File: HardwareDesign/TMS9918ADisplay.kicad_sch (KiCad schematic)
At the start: 21 parts, among them J701 Conn_01x02, Q701 2N4401, U701 TMS9918A, U702 74HCT04, U703 74HCT00, U704 74HCT574, U705 74HCT574, U706 74HCT574, U707 HM62256BLP-7, Y701 10.738635 MHz

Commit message: fix connections to data bus
TI stupidly uses "CD0" to mean the *most* significant bit of
the data bus, which is completely backwards.
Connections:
- net D0: now also U701.17 (CD7); no longer U701.24 (CD0)
- net D1: now also U701.18 (CD6); no longer U701.23 (CD1)
- net D2: now also U701.19 (CD5); no longer U701.22 (CD2)
- net D3: now also U701.20 (CD4); no longer U701.21 (CD3)
- net D4: now also U701.21 (CD3); no longer U701.20 (CD4)
- net D5: now also U701.22 (CD2); no longer U701.19 (CD5)
- net D6: now also U701.23 (CD1); no longer U701.18 (CD6)
- net D7: now also U701.24 (CD0); no longer U701.17 (CD7)

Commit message: prepare to create PCB for TMS9918A module
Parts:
- removed J701: Conn_01x02, symbol Connector_Generic:Conn_01x02
- added J701: RCJ-044, CUI_RCJ-044:CUI_RCJ-044, symbol RCJ-044:RCJ-044
- C701, C702, C703, C704, C705, C706, C707, C710, C711: footprint (none) -> Capacitor_THT:C_Disc_D3.4mm_W2.1mm_P2.50mm
- Q701: footprint (none) -> Package_TO_SOT_THT:TO-92_HandSolder
- R701, R702: footprint (none) -> Resistor_THT:R_Axial_DIN0207_L6.3mm_D2.5mm_P7.62mm_Horizontal
- U701: footprint (none) -> Package_DIP:DIP-40_W25.4mm_Socket
- U702, U703: footprint (none) -> Package_DIP:DIP-14_W7.62mm_Socket
- U704, U705, U706: footprint (none) -> Package_DIP:DIP-20_W7.62mm_Socket
- U707: footprint DIP28 -> Package_DIP:DIP-28_W7.62mm_Socket
- Y701: footprint (none) -> Crystal:Crystal_HC18-U_Vertical
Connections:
- net GND: now also J701.1
- net at Q701.1 (E), R702.1: now also J701.2

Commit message: add support for VDP interrupt
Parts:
- added J702: Conn_01x02, symbol Connector_Generic:Conn_01x02
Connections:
- net at U701.16 (~{INT}): now also J702.2 (Pin_2)
- new net ~{VDPINT}: J702.1 (Pin_1)
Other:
- note added: "Use a shorting block to connect VDP's interrupt output to a system IRQ input"
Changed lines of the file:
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@@
+    (stroke (width 0) (type default) (color 0 0 0 0))
+  )
+  (wire (pts (xy 50.8 71.12) (xy 36.83 71.12))
     (stroke (width 0) (type default) (color 0 0 0 0))
   )
@@
     (stroke (width 0) (type default) (color 0 0 0 0))
   )
+  (wire (pts (xy 26.67 24.13) (xy 36.83 24.13))
+    (stroke (width 0) (type default) (color 0 0 0 0))
+  )
   (wire (pts (xy 50.8 158.75) (xy 57.15 158.75))
     (stroke (width 0) (type default) (color 0 0 0 0))
@@
   )
   (wire (pts (xy 26.67 45.72) (xy 50.8 45.72))
+    (stroke (width 0) (type default) (color 0 0 0 0))
+  )
+  (wire (pts (xy 36.83 71.12) (xy 36.83 26.67))
     (stroke (width 0) (type default) (color 0 0 0 0))
   )
@@
     (effects (font (size 1.27 1.27)) (justify left bottom))
   )
+  (text "Use a shorting block to\nconnect VDP's interrupt output\nto a system IRQ input"
+    (at 30.48 20.32 0)
+    (effects (font (size 1.27 1.27)) (justify left bottom))
+  )
   (label "VA6" (at 171.45 105.41 0)
     (effects (font (size 1.27 1.27)) (justify left bottom))
@@
   )
   (hierarchical_label "D0" (shape bidirectional) (at 26.67 55.88 180)
+    (effects (font (size 1.27 1.27)) (justify right))
+  )
+  (hierarchical_label "~{VDPINT}" (shape output) (at 26.67 24.13 180)
     (effects (font (size 1.27 1.27)) (justify right))
   )
@@
     (pin "7")
   )
+  (symbol (lib_id "Connector_Generic:Conn_01x02") (at 41.91 24.13 0) (unit 1)
+    (in_bom yes) (on_board yes) (fields_autoplaced)
+    (property "Reference" "J702" (id 0) (at 44.45 24.1299 0)
+      (effects (font (size 1.27 1.27)) (justify left))
+    )
+    (property "Value" "Conn_01x02" (id 1) (at 44.45 26.6699 0)
+      (effects (font (size 1.27 1.27)) (justify left))
+    )
+    (property "Footprint" "" (id 2) (at 41.91 24.13 0)
+      (effects (font (size 1.27 1.27)) hide)
+    )
+    (property "Datasheet" "~" (id 3) (at 41.91 24.13 0)
+      (effects (font (size 1.27 1.27)) hide)
+    )
+    (pin "1")
+    (pin "2")
+  )
   (symbol (lib_id "74xx:74HCT00") (at 64.77 156.21 0) (unit 3)

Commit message: footprint for VDP interrupt enable jumper
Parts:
- J702: footprint (none) -> Connector_PinHeader_2.54mm:PinHeader_1x02_P2.54mm_Vertical
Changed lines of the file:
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@@
       (effects (font (size 1.27 1.27)) (justify left))
     )
-    (property "Footprint" "" (id 2) (at 41.91 24.13 0)
+    (property "Footprint" "Connector_PinHeader_2.54mm:PinHeader_1x02_P2.54mm_Vertical" (id 2) (at 41.91 24.13 0)
       (effects (font (size 1.27 1.27)) hide)
     )

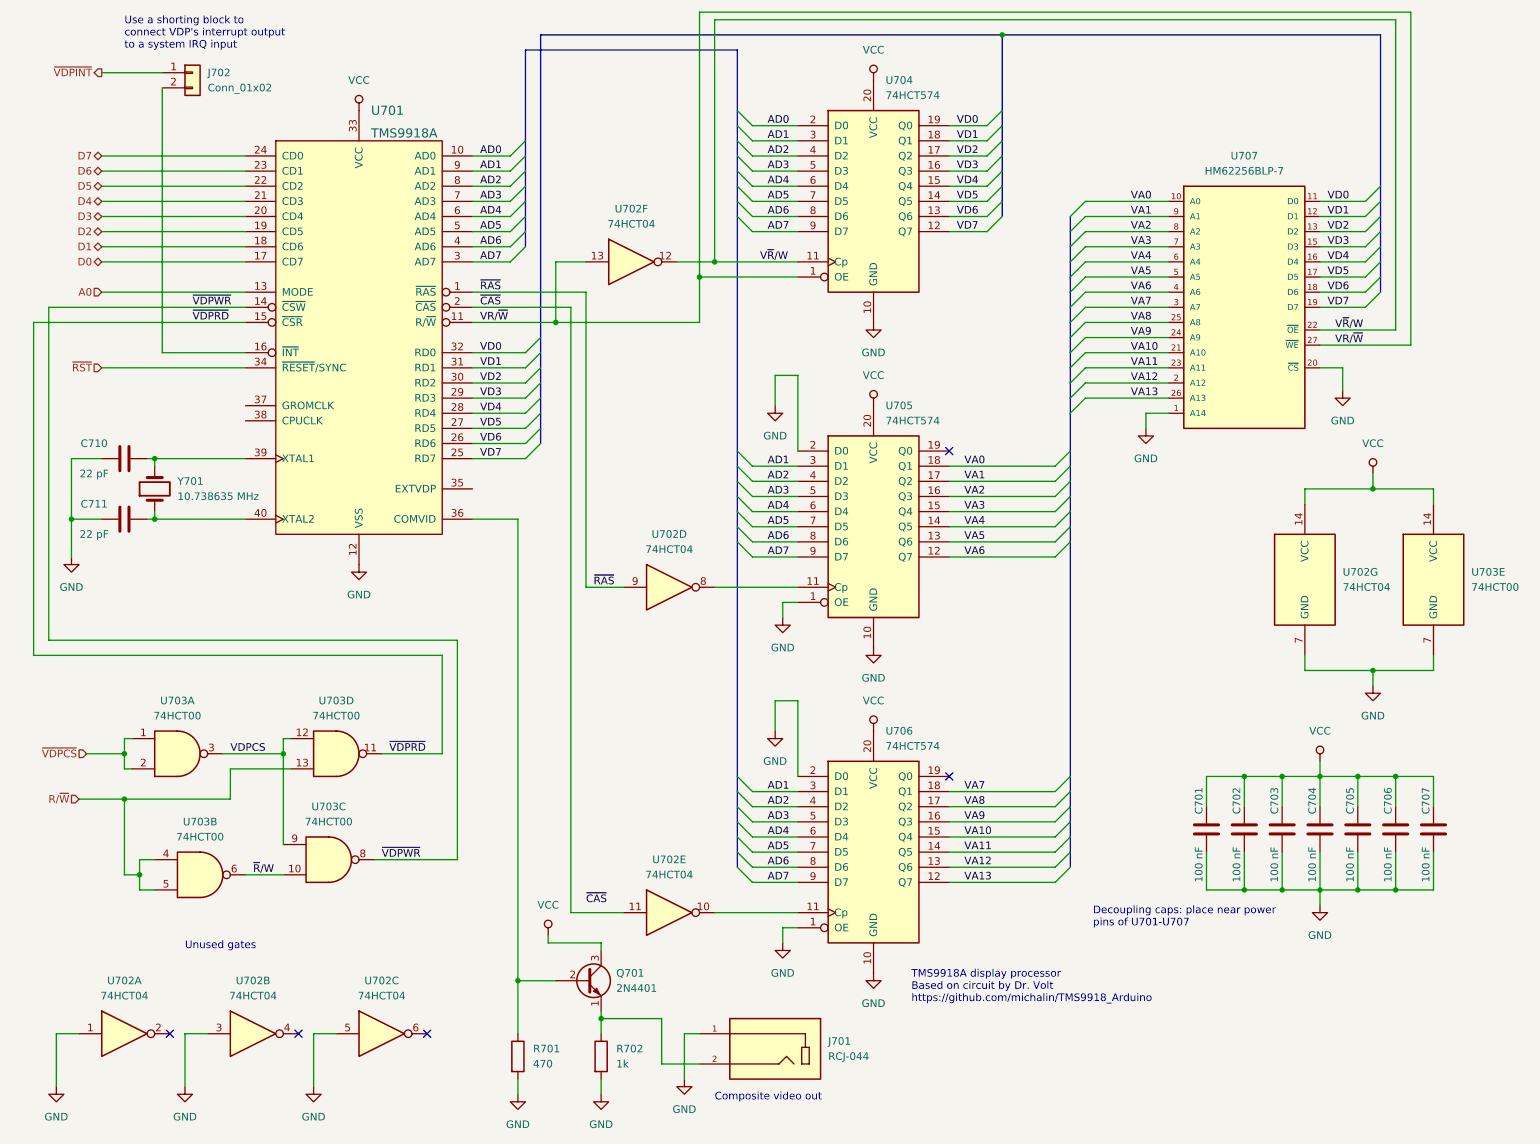
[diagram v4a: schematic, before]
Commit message: lots of changes to TMS9918A and YM2149 modules
Changed the TMS9918A circuit to use -RMEM and -WMEM rather than R/-W,
since -RMEM and -WMEM are properly synchronized with E and the overall
CPU bus cycle. (Duh!)

Also chnaged the YM2149 circuit to use -RMEM and -WMEM. However,
it's less clear that this is a desirable change, because we would
like BDIR and BC1 to change "at the same time", and only when
the chip is being accessed. However, if the chip select is asserted
before -RMEM/-WMEM are asserted, then meaningless BDIR and BC1
values are going to be generated, which is not good. Need to think
about this.
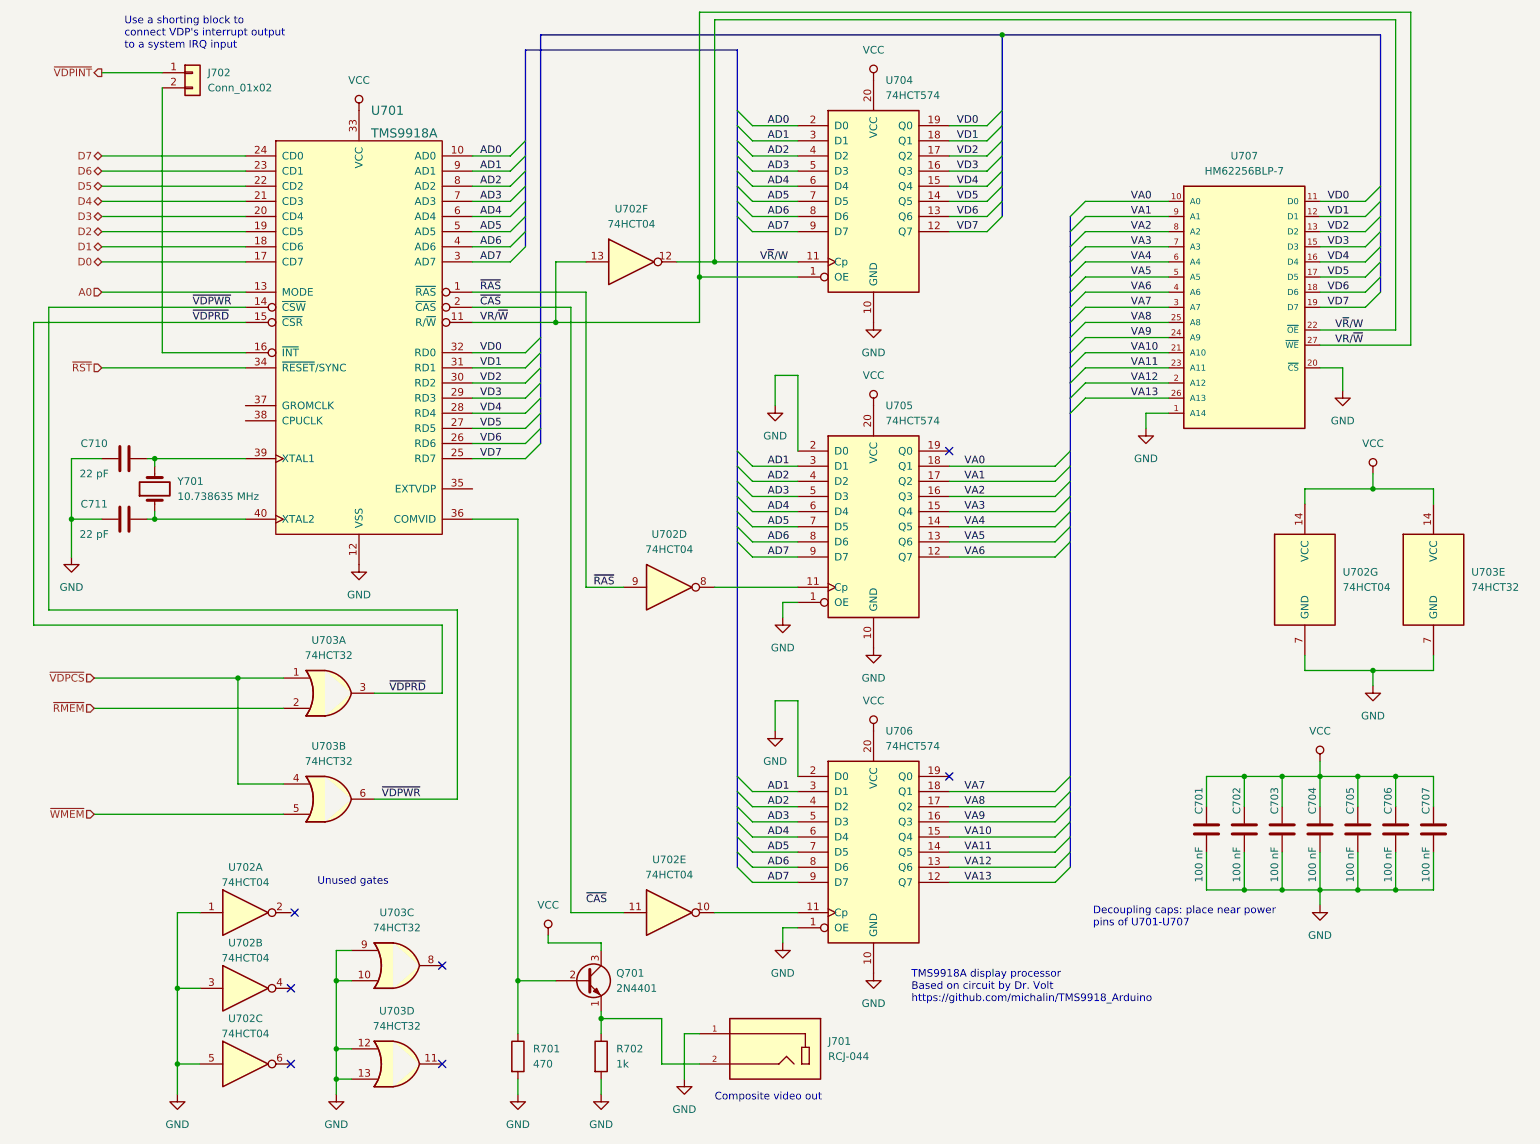
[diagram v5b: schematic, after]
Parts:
- removed U703: 74HCT00, Package_DIP:DIP-14_W7.62mm_Socket, symbol 74xx:74HCT00
- added U703: 74HCT32, symbol 74xx:74LS32
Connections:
- net GND: now also U703.10, U703.12, U703.13, U703.7 (GND), U703.9
- net VCC: now also U703.14 (VCC)
- net ~{VDPCS}: now also U703.1, U703.4
- net ~{VDPRD}: now also U703.3
- net ~{VDPWR}: now also U703.6
- new net ~{RMEM}: U703.2
- new net ~{WMEM}: U703.5
- no-connect marks 5 -> 7
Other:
- moved on the sheet: U702B, U702C

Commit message: footprint assignments for TMS9918A/YM2149 modules
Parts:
- U703: footprint (none) -> Package_DIP:DIP-14_W7.62mm_Socket
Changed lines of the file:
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@@
       (effects (font (size 1.27 1.27)) (justify left))
     )
-    (property "Footprint" "" (id 2) (at 250.19 109.22 0)
+    (property "Footprint" "Package_DIP:DIP-14_W7.62mm_Socket" (id 2) (at 250.19 109.22 0)
       (effects (font (size 1.27 1.27)) hide)
     )
@@
   (symbol (lib_id "power:GND") (at 66.04 195.58 0) (unit 1)
     (in_bom yes) (on_board yes) (fields_autoplaced)
-    (property "Reference" "#PWR?" (id 0) (at 66.04 201.93 0)
+    (property "Reference" "#PWR0214" (id 0) (at 66.04 201.93 0)
       (effects (font (size 1.27 1.27)) hide)
     )
@@
     (property "Reference" "U703" (id 0) (at 64.77 137.16 0))
     (property "Value" "74HCT32" (id 1) (at 64.77 139.7 0))
-    (property "Footprint" "" (id 2) (at 64.77 146.05 0)
+    (property "Footprint" "Package_DIP:DIP-14_W7.62mm_Socket" (id 2) (at 64.77 146.05 0)
       (effects (font (size 1.27 1.27)) hide)
     )
@@
     (property "Reference" "U703" (id 0) (at 64.77 119.38 0))
     (property "Value" "74HCT32" (id 1) (at 64.77 121.92 0))
-    (property "Footprint" "" (id 2) (at 64.77 128.27 0)
+    (property "Footprint" "Package_DIP:DIP-14_W7.62mm_Socket" (id 2) (at 64.77 128.27 0)
       (effects (font (size 1.27 1.27)) hide)
     )
@@
     (property "Reference" "U703" (id 0) (at 76.2 165.1 0))
     (property "Value" "74HCT32" (id 1) (at 76.2 167.64 0))
-    (property "Footprint" "" (id 2) (at 76.2 173.99 0)
+    (property "Footprint" "Package_DIP:DIP-14_W7.62mm_Socket" (id 2) (at 76.2 173.99 0)
       (effects (font (size 1.27 1.27)) hide)
     )
@@
     (property "Reference" "U703" (id 0) (at 76.2 181.61 0))
     (property "Value" "74HCT32" (id 1) (at 76.2 184.15 0))
-    (property "Footprint" "" (id 2) (at 76.2 190.5 0)
-      (effects (font (size 1.27 1.27)) hide)
-    )
+    (property "Footprint" "Package_DIP:DIP-14_W7.62mm_Socket" (id 2) (at 76.2 190.5 0)
+      (effects (font (size 1.27 1.27)) hide)
+    )

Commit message: fix some footprint assignments
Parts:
- U701: footprint Package_DIP:DIP-40_W25.4mm_Socket -> Package_DIP:DIP-40_W15.24mm_Socket
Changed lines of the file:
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@@
       (effects (font (size 1.524 1.524)) (justify left))
     )
-    (property "Footprint" "Package_DIP:DIP-40_W25.4mm_Socket" (id 2) (at 71.12 66.04 0)
+    (property "Footprint" "Package_DIP:DIP-40_W15.24mm_Socket" (id 2) (at 71.12 66.04 0)
       (effects (font (size 1.524 1.524)) hide)
     )

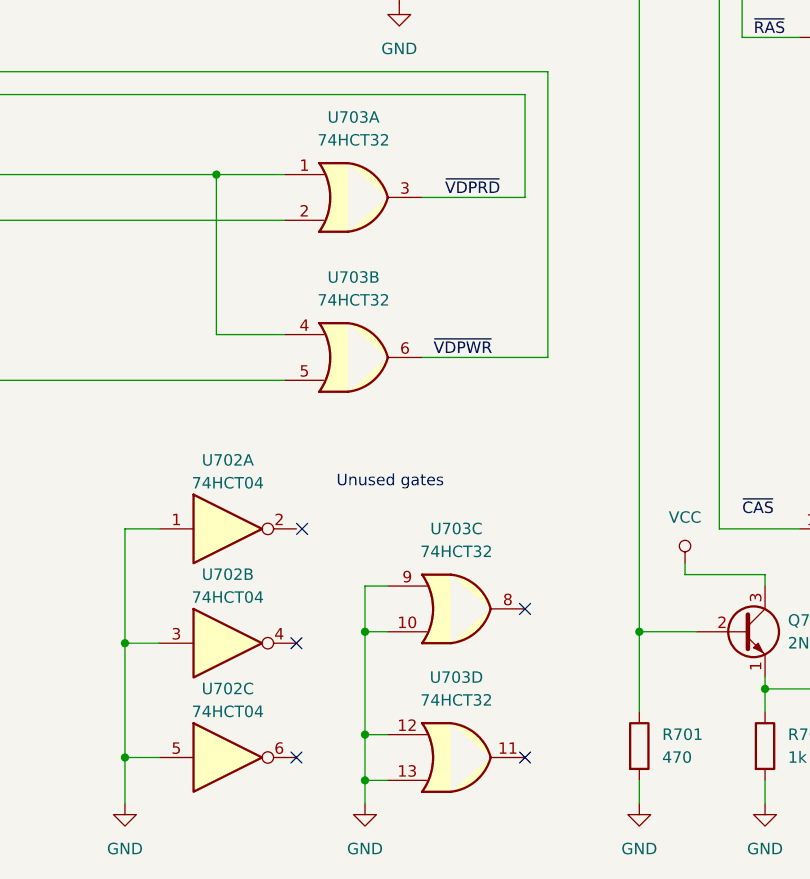
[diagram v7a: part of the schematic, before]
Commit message: initial schematic for FPGA display controller
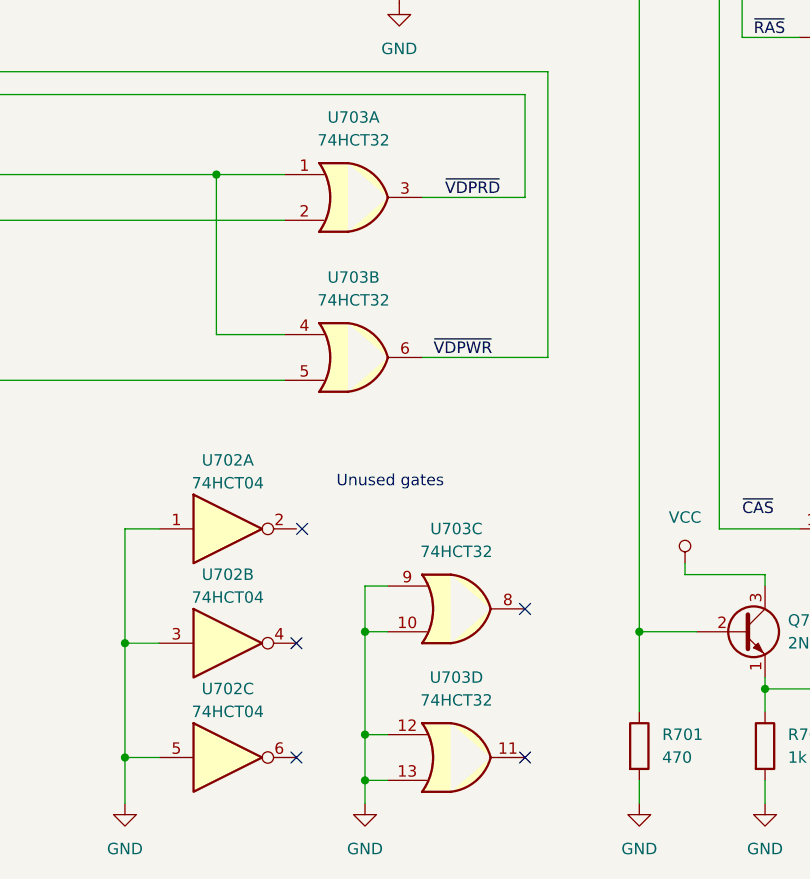
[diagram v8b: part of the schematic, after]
